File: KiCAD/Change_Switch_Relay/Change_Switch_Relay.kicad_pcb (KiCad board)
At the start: 2 copper layers, 71.6 x 76.2 mm, 19 parts, among them P1 1, P2 2, P3 Green, P4 Light Blue, P5 Green/Black, P6 12V, P7 Starter, Q1 2N3904, Q2 2N3904

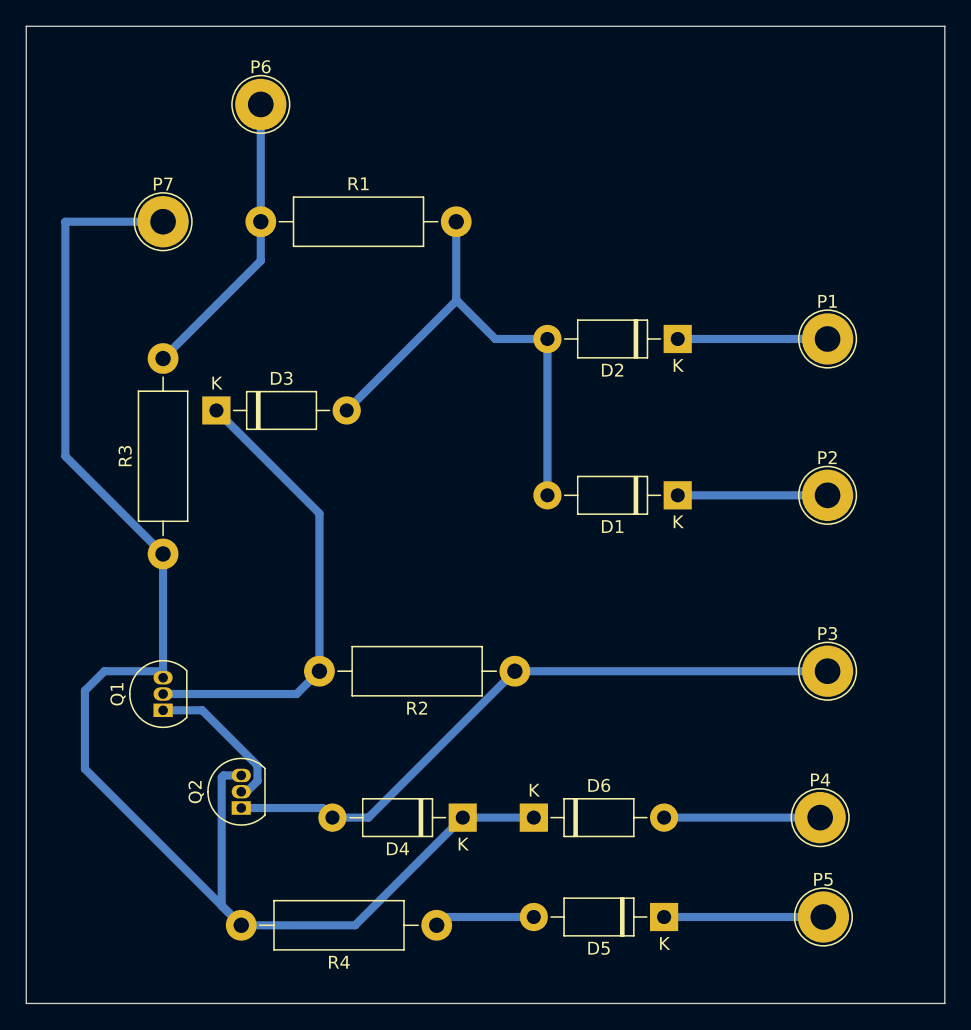
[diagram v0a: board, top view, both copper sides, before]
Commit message: Change Q1/Q2 to a single IR540NPBF MOSFET. Change R1 to 1K and R2 to 10K.
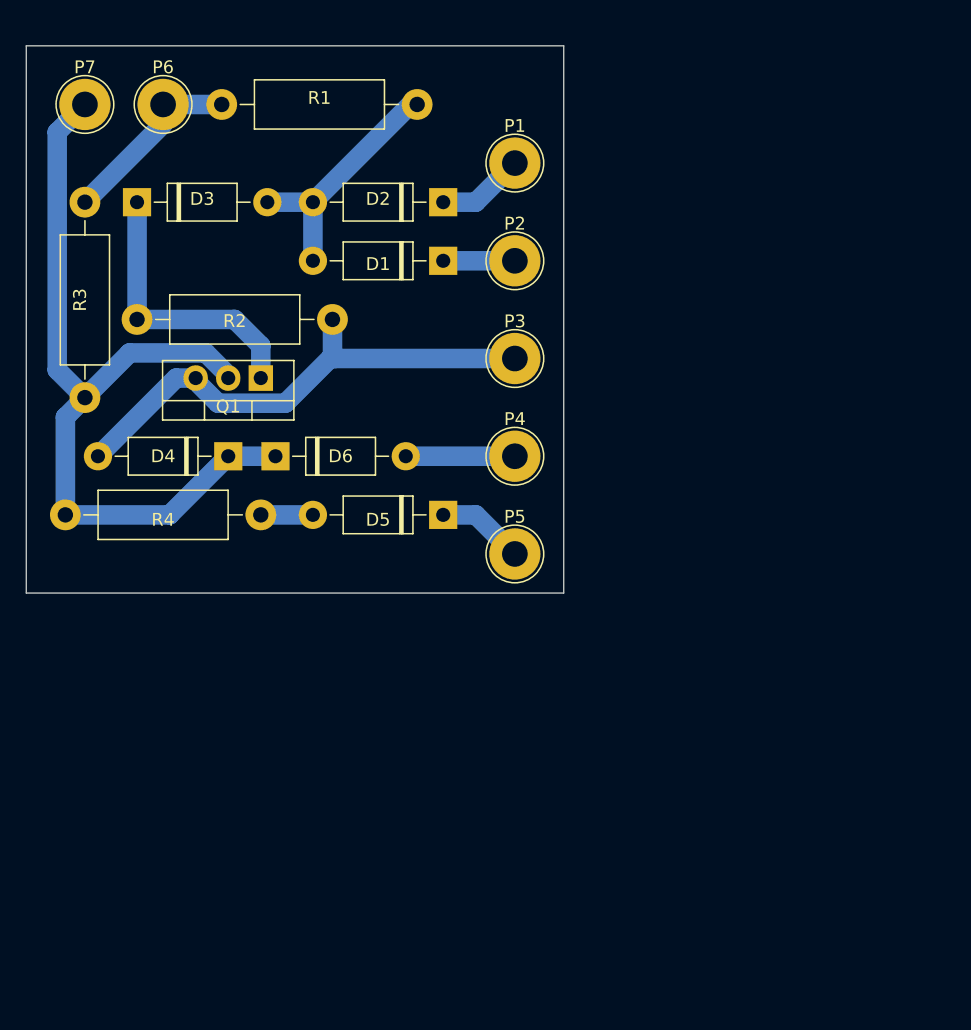
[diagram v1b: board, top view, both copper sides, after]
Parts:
- removed Q2: 2N3904, Package_TO_SOT_THT:TO-92_Inline
- Q1: value 2N3904 -> IRF540N; footprint Package_TO_SOT_THT:TO-92_Inline -> Package_TO_SOT_THT:TO-220-3_Vertical
- R1: value 630 -> 1K
- R2: value 1K -> 10K
- moved P5 37.2 mm to (123.4, 91.4)
- moved P4 36.9 mm to (123.4, 83.8)
- moved D5 35.8 mm to (117.9, 88.4)
- moved R4 34.8 mm to (103.6, 88.4)
- moved D6 34.6 mm to (104.8, 83.8)
- moved P3 34.5 mm to (123.4, 76.2)
- moved D4 33.6 mm to (101.1, 83.8)
- moved R2 30.9 mm to (109.2, 73.2)
- moved P2 30.5 mm to (123.4, 68.6)
- moved P1 28.0 mm to (123.4, 61.0)
- moved Q1 27.0 mm to (103.6, 77.7), turned to 180 degrees
- moved D1 25.9 mm to (117.9, 68.6)
- moved D2 21.2 mm to (117.9, 64.0)
- moved D3 17.4 mm to (94.0, 64.0)
- moved R3 13.6 mm to (89.9, 79.2)
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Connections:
- D4 pad 1: Net-(Q1-Pad3) -> Net-(D4-Pad1)
- D6 pad 1: Net-(Q1-Pad3) -> Net-(D4-Pad1)
- P7 pad 1: Net-(Q1-Pad3) -> Net-(D4-Pad1)
- Q1 pad 1: Net-(Q1-Pad1) -> Net-(D3-Pad1)
- Q1 pad 2: Net-(D3-Pad1) -> Net-(D4-Pad1)
- Q1 pad 3: Net-(Q1-Pad3) -> Net-(D4-Pad2)
- R3 pad 1: Net-(Q1-Pad3) -> Net-(D4-Pad1)
- R4 pad 2: Net-(Q1-Pad3) -> Net-(D4-Pad1)
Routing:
- net Net-(Q1-Pad3): track 116.4 -> 0.00 mm
- net Net-(D4-Pad1): track 0.00 -> 66.3 mm
- net Net-(D1-Pad2): track 38.8 -> 19.4 mm
- net Net-(D3-Pad1): track 36.6 -> 22.2 mm
- net Net-(Q1-Pad1): track 12.0 -> 0.00 mm
- net Net-(D4-Pad2): track 50.8 -> 40.4 mm
- net Net-(P6-Pad1): track 23.0 -> 14.7 mm
- net Net-(D1-Pad1): track 11.7 -> 5.59 mm
- net Net-(D5-Pad1): track 12.4 -> 6.85 mm
- net Net-(D2-Pad1): track 11.7 -> 6.85 mm
- net Net-(D5-Pad2): track 7.84 -> 4.06 mm
- net Net-(D6-Pad2): track 12.2 -> 8.51 mm
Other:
- board size 71.6 x 76.2 mm -> 41.9 x 42.7 mm

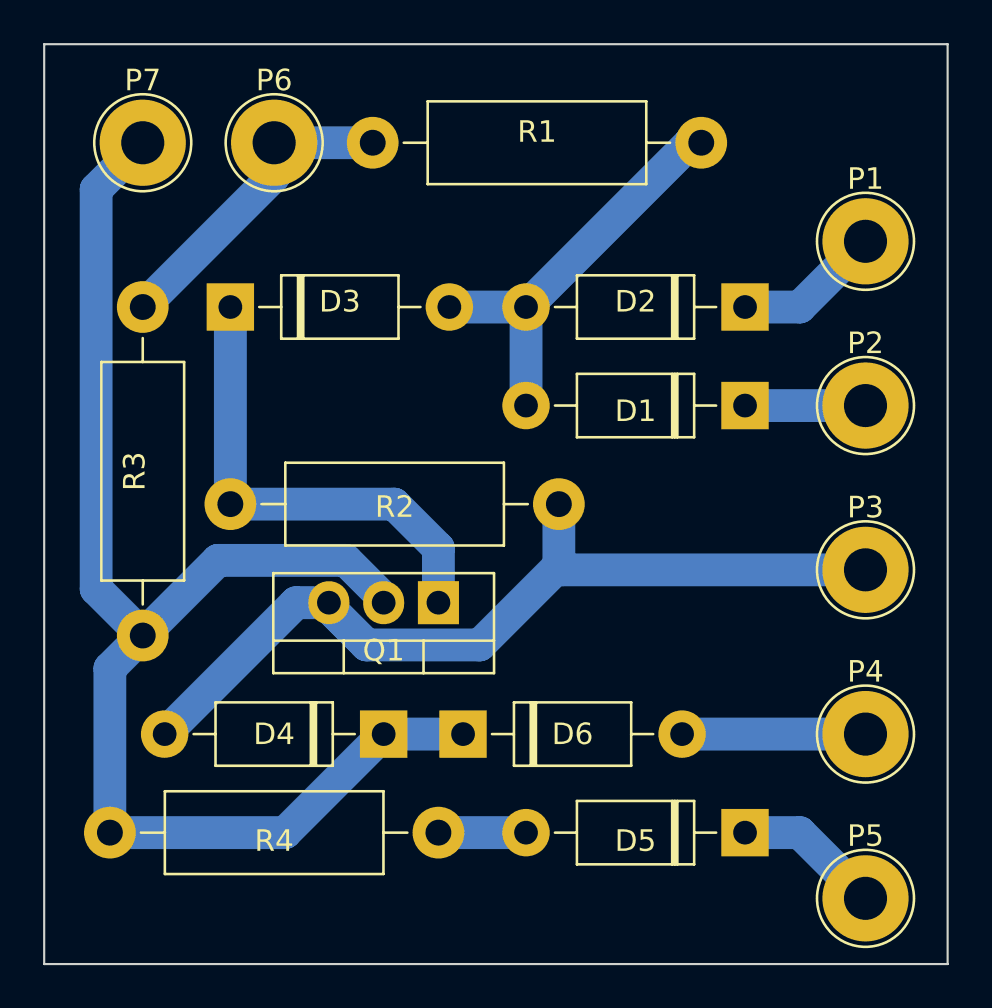
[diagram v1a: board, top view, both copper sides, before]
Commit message: Shrink Change Relay PCB size down to the original with through hole components.
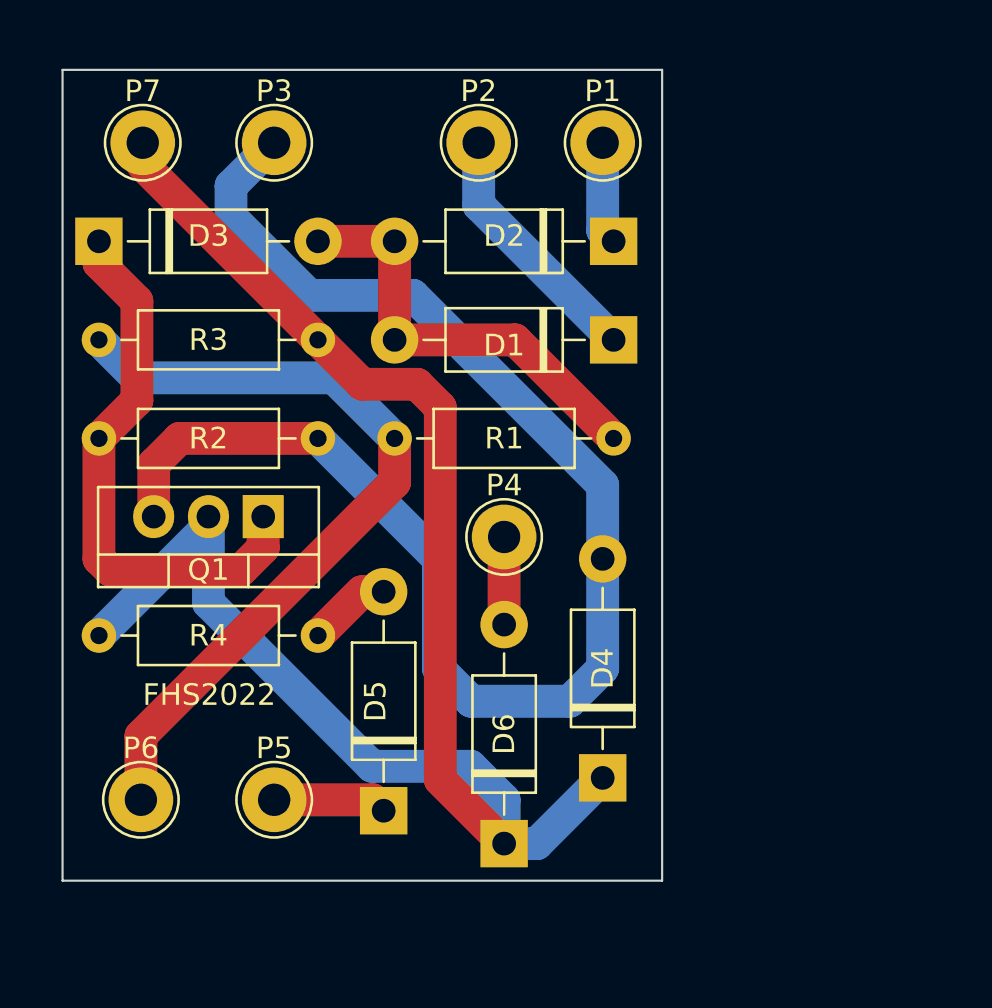
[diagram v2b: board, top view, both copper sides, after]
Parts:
- P1, P2, P3, P4, P5, P6, P7: footprint TestPoint:TestPoint_THTPad_D4.0mm_Drill2.0mm -> TestPoint:TestPoint_THTPad_D3.0mm_Drill1.5mm
- R1, R2, R3, R4: footprint Resistor_THT:R_Axial_DIN0411_L9.9mm_D3.6mm_P15.24mm_Horizontal -> Resistor_THT:R_Axial_DIN0207_L6.3mm_D2.5mm_P10.16mm_Horizontal
- moved P3 33.8 mm to (96.0, 56.4)
- moved P6 31.1 mm to (89.8, 86.9)
- moved P5 27.8 mm to (96.0, 86.9)
- moved P2 21.7 mm to (105.5, 56.4)
- moved P4 19.1 mm to (106.7, 74.7)
- moved D5 16.8 mm to (101.1, 87.4), turned to 90 degrees
- moved R3 15.9 mm to (98.0, 65.5), turned to 180 degrees
- moved R1 13.8 mm to (101.6, 70.1)
- moved P1 13.0 mm to (111.3, 56.4)
- moved R2 11.6 mm to (98.0, 70.1)
- moved R4 10.7 mm to (98.0, 79.2)
- moved D4 10.4 mm to (111.3, 85.9), turned to 90 degrees
- moved Q1 9.06 mm to (95.5, 73.7)
- moved D3 6.82 mm to (87.9, 61.0)
- moved D1 6.82 mm to (111.8, 65.5)
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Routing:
- net Net-(D4-Pad2): track 40.4 -> 67.6 mm
- net Net-(P6-Pad1): track 14.7 -> 37.2 mm
- net Net-(D4-Pad1): track 66.3 -> 76.9 mm
- net Net-(D1-Pad1): track 5.59 -> 11.7 mm
- net Net-(D6-Pad2): track 8.51 -> 4.06 mm
- net Net-(D3-Pad1): track 22.2 -> 25.9 mm
- net Net-(D2-Pad1): track 6.85 -> 4.78 mm
- net Net-(D5-Pad1): track 6.85 -> 5.29 mm
- net Net-(D1-Pad2): track 19.4 -> 20.2 mm
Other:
- board size 41.9 x 42.7 mm -> 27.8 x 37.6 mm
- board text added: "FHS2022"
